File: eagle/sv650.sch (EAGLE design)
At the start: 17 parts, among them IC1 7805T

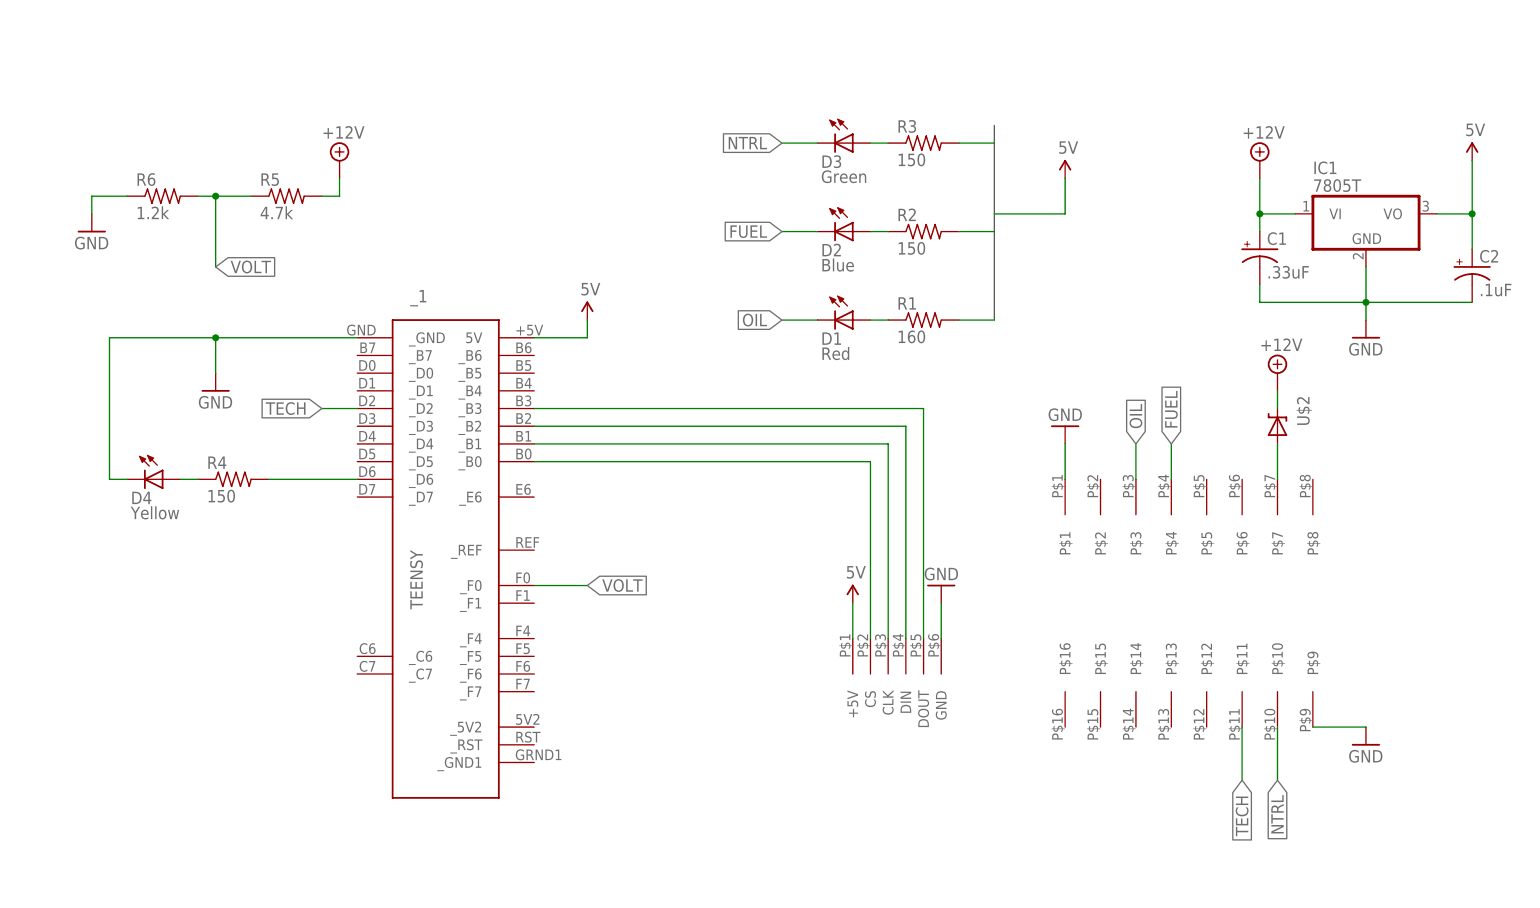
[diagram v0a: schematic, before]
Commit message: improve board layout and update resistor divider circuit
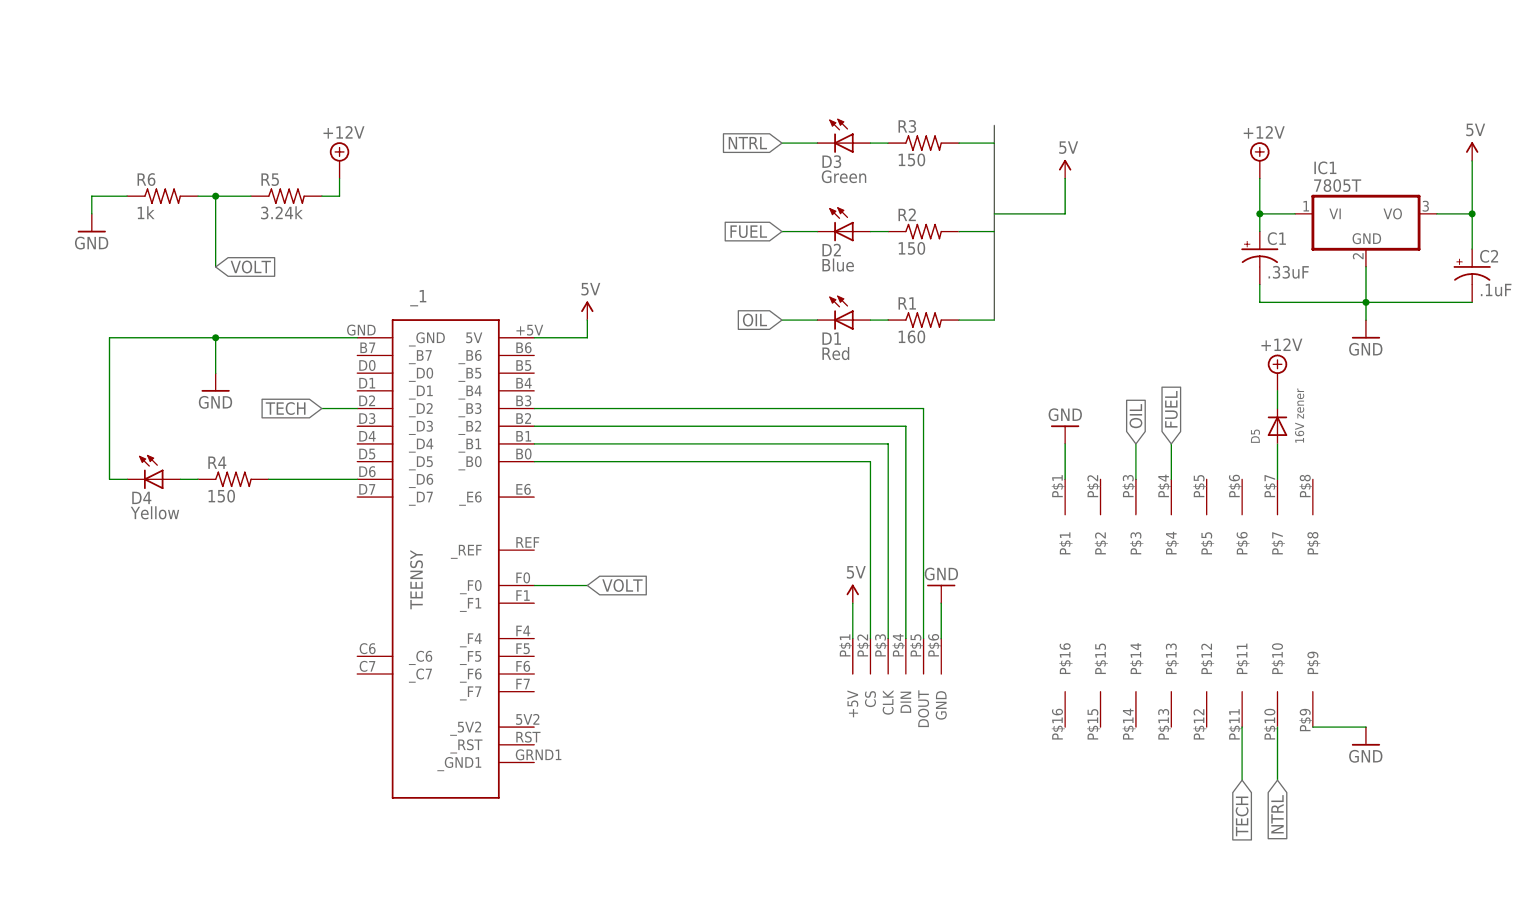
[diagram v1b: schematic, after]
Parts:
- removed U$2: BZT52C20-7-F 20V, SparkFun:DIODE-ZENER-BZT52
- added D5: 16V zener, adafruit:DIODESOD-123
- C1, C2, D1, D2, D3, D4, IC1, R1, R2, R3, R4, U$1, U$3, _1: OC_NEWARK (none) -> unknown
- R5: value 4.7k -> 3.24k; OC_NEWARK (none) -> unknown
- R6: value 1.2k -> 1k; OC_NEWARK (none) -> unknown
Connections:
- net +12V: now also D5.C; no longer U$2.C
- net N$1: now also D5.A; no longer U$2.A

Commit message: add .gitignore Update schema and board with updated connector, resistors for voltage divider and zener.
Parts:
- D5: value 16V zener -> 15V zener
- R5: value 3.24k -> 32.4k
- R6: value 1k -> 10k
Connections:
- net VOLT renamed ADC
- removed net N$1: D5.A, U$3.P$7
- net +12V: now also U$3.P$7
- net GND: now also D5.A, _1._GND1
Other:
- moved on the sheet: D4, D5, R4, R5, R6

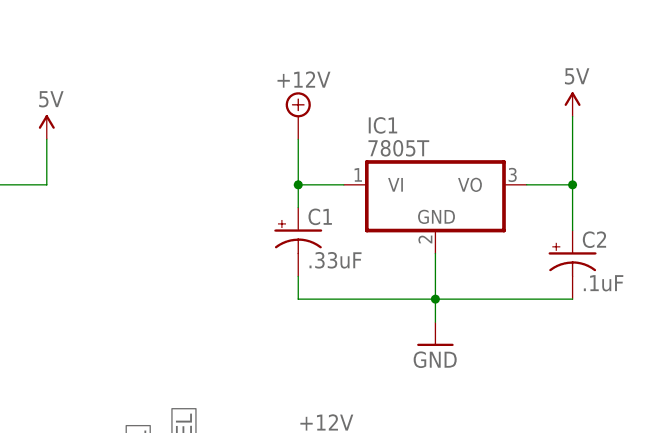
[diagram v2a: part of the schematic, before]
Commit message: update layout of 7805 to use a pad for solder not drill hole for hard mounting.  Update silkscreen and improve layout for sending to OshPark for fabrication.
Just waiting on feedback on voltage divider & zener.
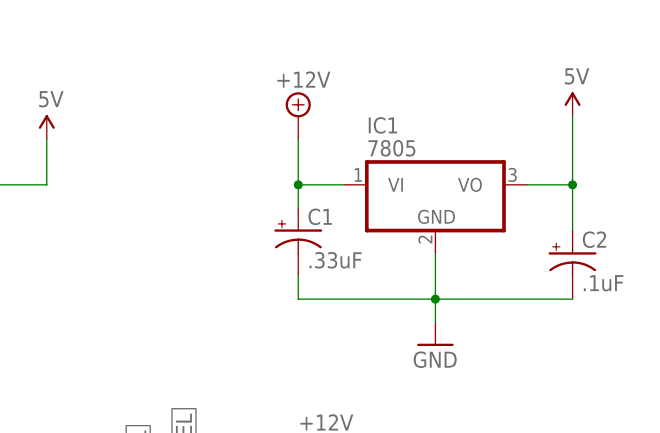
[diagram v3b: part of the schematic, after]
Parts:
- IC1: value 7805T -> 7805; device linear:7805T -> linear:78TH2
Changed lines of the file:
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@@
 </classes>
 <parts>
-<part name="IC1" library="linear" deviceset="78*" device="T" technology="05">
+<part name="IC1" library="linear" deviceset="78*" device="TH2" value="7805">
 <attribute name="MF" value=""/>
 <attribute name="MPN" value=""/>

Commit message: board as ordered from OshPark for v4.0
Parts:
- removed D5: 15V zener, adafruit:DIODESOD-123
- added D6: 12V zener, adafruit:DIODESOD-123
- added R8: 10k, resistor:R-US_M0805
- C1, C2: device SparkFun:CAP_POL1206 -> adafruit:C-US025-024X044
- R1: MF (none) -> VISHAY/DALE; MPN (none) -> CRCW0805160RFKEA; OC_NEWARK unknown -> 52K9907
- R2, R3, R4: MPN (none) -> MCHP05W4F1500T5E; OC_NEWARK unknown -> 01N7000
- R5: value 32.4k -> 22k; MPN (none) -> CRCW080522K0FKEA; OC_NEWARK unknown -> 61M5466
- R6: MF (none) -> VISHAY/DALE; MPN (none) -> CRCW080510K0FKTA; OC_NEWARK unknown -> 05F1511
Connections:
- new net N$13: D6.C, R5.2, R8.1
- net +12V: now also C1.1, R8.2; no longer C1.+, D5.C, R5.2
- net 5V: now also C2.1; no longer C2.+
- net GND: now also C1.2, C2.2, D6.A; no longer C1.-, C2.-, D5.A
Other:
- moved on the sheet: D1, D2, D3, D4, IC1, R1, R2, R3, R4, R5, R6, _1

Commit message: update board & schema to v4.1 - Add 5V zener to protect ADC from shorts - Add .1uF cap to even out ADC line from noise - Tweak placement of low fuel LED - Tweak placement of S/N: XXXXXX
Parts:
- added C3: .1uF, adafruit:C-US025-024X044
- added D5: 5V zener, adafruit:DIODESOD-123
- D6: value 12V zener -> 20V zener
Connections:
- net +12V: now also U$3.P$8; no longer U$3.P$7
- net ADC: now also C3.1, D5.C
- net GND: now also C3.2, D5.A; no longer _1._GND1
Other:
- note added: "650 ECU Decoder v4.1"
- note added: "To Wiring Harness"
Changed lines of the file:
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@@
 <part name="SUPPLY1" library="supply2" deviceset="+12V" device=""/>
 <part name="SUPPLY2" library="supply2" deviceset="+12V" device=""/>
-<part name="GND7" library="SparkFun" deviceset="GND" device=""/>
 <part name="R8" library="resistor" deviceset="R-US_" device="M0805" value="10k">
 <attribute name="MF" value="VISHAY/DALE"/>
@@
 <attribute name="OC_NEWARK" value="05F1511"/>
 </part>
-<part name="D6" library="adafruit" deviceset="DIODE" device="SOD-123" value="12V zener">
+<part name="D6" library="adafruit" deviceset="DIODE" device="SOD-123" value="20V zener">
 <attribute name="MF" value="VISHAY/TELEFUNKEN"/>
 <attribute name="MPN" value="MMSZ5242B-V-GS08"/>
@@
 <part name="SUPPLY3" library="supply2" deviceset="+12V" device=""/>
 <part name="GND2" library="SparkFun" deviceset="GND" device=""/>
+<part name="D5" library="adafruit" deviceset="DIODE" device="SOD-123" value="5V zener">
+<attribute name="MF" value="VISHAY/TELEFUNKEN"/>
+<attribute name="MPN" value="MMSZ5242B-V-GS08"/>
+<attribute name="OC_NEWARK" value="35K8677"/>
+</part>
+<part name="C3" library="adafruit" deviceset="C-US" device="025-024X044" value=".1uF">
+<attribute name="MF" value=""/>
+<attribute name="MPN" value=""/>
+<attribute name="OC_NEWARK" value="unknown"/>
+</part>
 </parts>
 <sheets>
 <sheet>
 <plain>
+<text x="114.3" y="68.58" size="1.778" layer="91" rot="R90">To Wiring Harness</text>
+<text x="-15.24" y="48.26" size="1.778" layer="91">650 ECU Decoder v4.1</text>
 </plain>
 <instances>
@@
 <instance part="SUPPLY1" gate="+12V" x="30.48" y="104.14"/>
 <instance part="SUPPLY2" gate="+12V" x="55.88" y="101.6"/>
-<instance part="GND7" gate="1" x="93.98" y="-7.62"/>
 <instance part="R8" gate="G$1" x="22.86" y="101.6">
 <attribute name="OC_NEWARK" x="22.86" y="101.6" size="1.778" layer="96" display="off"/>
@@
 <attribute name="MPN" x="10.16" y="93.98" size="1.778" layer="96" display="off"/>
 </instance>
-<instance part="SUPPLY3" gate="+12V" x="149.86" y="106.68"/>
-<instance part="GND2" gate="1" x="-7.62" y="78.74"/>
+<instance part="SUPPLY3" gate="+12V" x="154.94" y="109.22"/>
+<instance part="GND2" gate="1" x="-7.62" y="63.5"/>
+<instance part="D5" gate="G$1" x="-20.32" y="88.9">
+<attribute name="OC_NEWARK" x="-20.32" y="88.9" size="1.778" layer="96" rot="R270" display="off"/>
+<attribute name="MF" x="-20.32" y="88.9" size="1.778" layer="96" rot="R270" display="off"/>
+<attribute name="MPN" x="-20.32" y="88.9" size="1.778" layer="96" rot="R270" display="off"/>
+</instance>
+<instance part="C3" gate="G$1" x="-17.78" y="76.2" rot="R270">
+<attribute name="OC_NEWARK" x="-17.78" y="76.2" size="1.778" layer="96" rot="R270" display="off"/>
+<attribute name="MF" x="-17.78" y="76.2" size="1.778" layer="96" rot="R270" display="off"/>
+<attribute name="MPN" x="-17.78" y="76.2" size="1.778" layer="96" rot="R270" display="off"/>
+</instance>
 </instances>
 <busses>
@@
 </segment>
 <segment>
-<pinref part="_1" gate="G$1" pin="_GND1"/>
-<pinref part="GND7" gate="1" pin="GND"/>
-<wire x1="91.44" y1="-2.54" x2="93.98" y2="-2.54" width="0.1524" layer="91"/>
-<wire x1="93.98" y1="-2.54" x2="93.98" y2="-5.08" width="0.1524" layer="91"/>
-</segment>
-<segment>
+<wire x1="-27.94" y1="66.04" x2="-7.62" y2="66.04" width="0.1524" layer="91"/>
+<pinref part="D6" gate="G$1" pin="A"/>
+<wire x1="-7.62" y1="66.04" x2="10.16" y2="66.04" width="0.1524" layer="91"/>
+<wire x1="10.16" y1="66.04" x2="10.16" y2="91.44" width="0.1524" layer="91"/>
+<pinref part="GND2" gate="1" pin="GND"/>
+<junction x="-7.62" y="66.04"/>
 <pinref part="R6" gate="G$1" pin="1"/>
 <wire x1="-22.86" y1="101.6" x2="-27.94" y2="101.6" width="0.1524" layer="91"/>
-<wire x1="-27.94" y1="101.6" x2="-27.94" y2="81.28" width="0.1524" layer="91"/>
-<wire x1="-27.94" y1="81.28" x2="-7.62" y2="81.28" width="0.1524" layer="91"/>
-<pinref part="D6" gate="G$1" pin="A"/>
-<wire x1="-7.62" y1="81.28" x2="10.16" y2="81.28" width="0.1524" layer="91"/>
-<wire x1="10.16" y1="81.28" x2="10.16" y2="91.44" width="0.1524" layer="91"/>
-<pinref part="GND2" gate="1" pin="GND"/>
-<junction x="-7.62" y="81.28"/>
+<wire x1="-27.94" y1="101.6" x2="-27.94" y2="88.9" width="0.1524" layer="91"/>
+<pinref part="D5" gate="G$1" pin="A"/>
+<wire x1="-22.86" y1="88.9" x2="-27.94" y2="88.9" width="0.1524" layer="91"/>
+<wire x1="-27.94" y1="88.9" x2="-27.94" y2="76.2" width="0.1524" layer="91"/>
+<pinref part="C3" gate="G$1" pin="2"/>
+<wire x1="-27.94" y1="76.2" x2="-27.94" y2="66.04" width="0.1524" layer="91"/>
+<wire x1="-27.94" y1="76.2" x2="-22.86" y2="76.2" width="0.1524" layer="91"/>
+<junction x="-27.94" y="76.2"/>
+<junction x="-27.94" y="88.9"/>
 </segment>
 </net>
@@
 </segment>
 <segment>
-<pinref part="U$3" gate="G$1" pin="P$7"/>
-<wire x1="149.86" y1="104.14" x2="149.86" y2="99.06" width="0.1524" layer="91"/>
 <pinref part="SUPPLY3" gate="+12V" pin="+12V"/>
+<pinref part="U$3" gate="G$1" pin="P$8"/>
+<wire x1="154.94" y1="106.68" x2="154.94" y2="99.06" width="0.1524" layer="91"/>
 </segment>
 </net>
@@
 </segment>
 <segment>
-<wire x1="-10.16" y1="101.6" x2="-10.16" y2="91.44" width="0.1524" layer="91"/>
 <pinref part="R5" gate="G$1" pin="1"/>
 <pinref part="R6" gate="G$1" pin="2"/>
 <wire x1="-2.54" y1="101.6" x2="-10.16" y2="101.6" width="0.1524" layer="91"/>
+<label x="-2.54" y="73.66" size="1.778" layer="95" xref="yes"/>
+<wire x1="-10.16" y1="101.6" x2="-12.7" y2="101.6" width="0.1524" layer="91"/>
 <junction x="-10.16" y="101.6"/>
-<wire x1="-10.16" y1="101.6" x2="-12.7" y2="101.6" width="0.1524" layer="91"/>
-<label x="-10.16" y="91.44" size="1.778" layer="95" xref="yes"/>
-</segment>
-</net>
+<wire x1="-10.16" y1="73.66" x2="-2.54" y2="73.66" width="0.1524" layer="91"/>
+<wire x1="-10.16" y1="101.6" x2="-10.16" y2="88.9" width="0.1524" layer="91"/>
+<pinref part="D5" gate="G$1" pin="C"/>
+<wire x1="-10.16" y1="88.9" x2="-10.16" y2="76.2" width="0.1524" layer="91"/>
+<wire x1="-10.16" y1="76.2" x2="-10.16" y2="73.66" width="0.1524" layer="91"/>
+<wire x1="-10.16" y1="88.9" x2="-17.78" y2="88.9" width="0.1524" layer="91"/>
+<junction x="-10.16" y="88.9"/>
+<junction x="-10.16" y="76.2"/>
+<pinref part="C3" gate="G$1" pin="1"/>
+<wire x1="-10.16" y1="76.2" x2="-15.24" y2="76.2" width="0.1524" layer="91"/>
+</segment>
+</net>
